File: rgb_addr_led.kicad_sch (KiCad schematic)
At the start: 64 parts

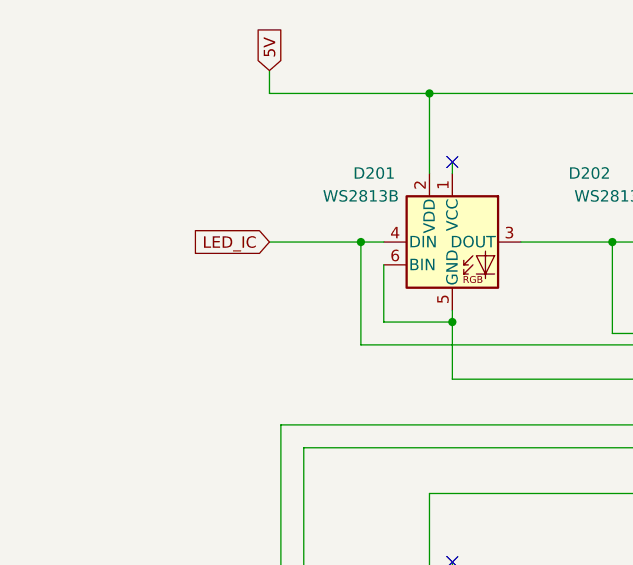
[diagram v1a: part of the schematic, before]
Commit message: add backup led data line with open solder bridge
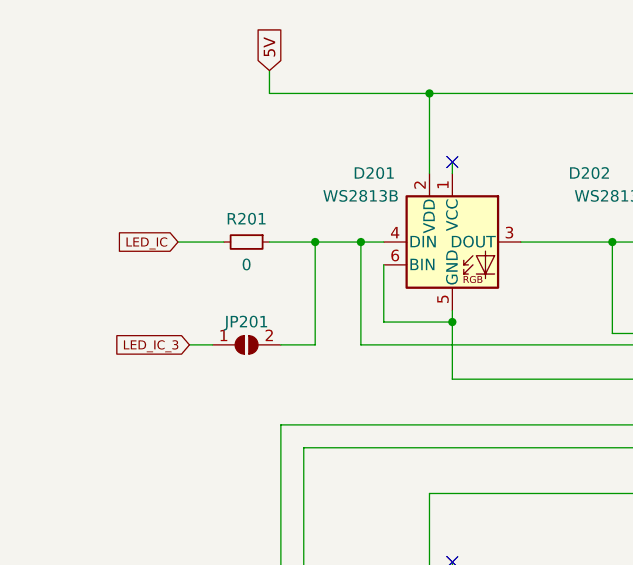
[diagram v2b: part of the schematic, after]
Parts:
- added JP201: SolderJumper_2_Open, Jumper:SolderJumper-2_P1.3mm_Open_TrianglePad1.0x1.5mm, symbol Jumper:SolderJumper_2_Open
- added R201: 0, Resistor_SMD:R_1206_3216Metric, symbol Device:R_Small
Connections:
- net LED_IC: now also R201.2; no longer D201.4 (DIN), D202.6 (BIN)
- new net: D201.4 (DIN), D202.6 (BIN), JP201.2 (B), R201.1
- new net LED_IC_3: JP201.1 (A)
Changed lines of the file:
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@@
   (junction (at 191.77 36.83) (diameter 0) (color 0 0 0 0)
   )
-  (junction (at 50.8 36.83) (diameter 0) (color 0 0 0 0)
-  )
   (junction (at 78.74 259.08) (diameter 0) (color 0 0 0 0)
   )
@@
   (junction (at 370.84 109.22) (diameter 0) (color 0 0 0 0)
   )
+  (junction (at 45.72 36.83) (diameter 0) (color 0 0 0 0)
+  )
   (junction (at 163.83 170.18) (diameter 0) (color 0 0 0 0)
   )
@@
   (junction (at 306.07 214.63) (diameter 0) (color 0 0 0 0)
   )
+  (junction (at 50.8 36.83) (diameter 0) (color 0 0 0 0)
+  )
   (junction (at 373.38 96.52) (diameter 0) (color 0 0 0 0)
   )
@@
     (stroke (width 0) (type default) (color 0 0 0 0))
   )
+  (wire (pts (xy 30.48 36.83) (xy 35.56 36.83))
+    (stroke (width 0) (type default) (color 0 0 0 0))
+  )
   (wire (pts (xy 78.74 214.63) (xy 78.74 224.79))
     (stroke (width 0) (type default) (color 0 0 0 0))
@@
     (stroke (width 0) (type default) (color 0 0 0 0))
   )
-  (wire (pts (xy 40.64 36.83) (xy 50.8 36.83))
-    (stroke (width 0) (type default) (color 0 0 0 0))
-  )
   (wire (pts (xy 344.17 27.94) (xy 344.17 29.21))
     (stroke (width 0) (type default) (color 0 0 0 0))
@@
     (stroke (width 0) (type default) (color 0 0 0 0))
   )
+  (wire (pts (xy 31.75 48.26) (xy 34.29 48.26))
+    (stroke (width 0) (type default) (color 0 0 0 0))
+  )
   (wire (pts (xy 308.61 48.26) (xy 278.13 48.26))
     (stroke (width 0) (type default) (color 0 0 0 0))
@@
     (stroke (width 0) (type default) (color 0 0 0 0))
   )
+  (wire (pts (xy 45.72 48.26) (xy 45.72 36.83))
+    (stroke (width 0) (type default) (color 0 0 0 0))
+  )
   (wire (pts (xy 41.91 81.28) (xy 49.53 81.28))
     (stroke (width 0) (type default) (color 0 0 0 0))
@@
     (stroke (width 0) (type default) (color 0 0 0 0))
   )
+  (wire (pts (xy 45.72 36.83) (xy 50.8 36.83))
+    (stroke (width 0) (type default) (color 0 0 0 0))
+  )
   (wire (pts (xy 116.84 250.19) (xy 116.84 251.46))
     (stroke (width 0) (type default) (color 0 0 0 0))
@@
     (stroke (width 0) (type default) (color 0 0 0 0))
   )
+  (wire (pts (xy 41.91 48.26) (xy 45.72 48.26))
+    (stroke (width 0) (type default) (color 0 0 0 0))
+  )
   (wire (pts (xy 256.54 153.67) (xy 256.54 162.56))
     (stroke (width 0) (type default) (color 0 0 0 0))
@@
     (stroke (width 0) (type default) (color 0 0 0 0))
   )
+  (wire (pts (xy 40.64 36.83) (xy 45.72 36.83))
+    (stroke (width 0) (type default) (color 0 0 0 0))
+  )
   (text "NOTE:" (at 13.97 77.47 0)
     (effects (font (size 1.27 1.27) (thickness 0.254) bold) (justify left bottom))
@@
     )
   )
-  (global_label "LED_IC" (shape input) (at 40.64 36.83 180) (fields_autoplaced)
-    (effects (font (size 1.27 1.27)) (justify right))
-    (property "Intersheet References" "${INTERSHEET_REFS}" (id 0) (at 31.9374 36.7506 0)
-      (effects (font (size 1.27 1.27)) (justify right) hide)
+  (global_label "LED_IC" (shape input) (at 30.48 36.83 180) (fields_autoplaced)
+    (effects (font (size 1 1)) (justify right))
+    (property "Intersheet References" "${INTERSHEET_REFS}" (id 0) (at 23.6276 36.7675 0)
+      (effects (font (size 1 1)) (justify right) hide)
+    )
+  )
+  (global_label "LED_IC_3" (shape input) (at 31.75 48.26 180) (fields_autoplaced)
+    (effects (font (size 1 1)) (justify right))
+    (property "Intersheet References" "${INTERSHEET_REFS}" (id 0) (at 23.1833 48.1975 0)
+      (effects (font (size 1 1)) (justify right) hide)
     )
   )
@@
     (pin "6")
   )
+  (symbol (lib_id "Device:R_Small") (at 38.1 36.83 270) (unit 1)
+    (in_bom yes) (on_board yes)
+    (property "Reference" "R201" (id 0) (at 38.1 34.29 90))
+    (property "Value" "0" (id 1) (at 38.1 39.37 90))
+    (property "Footprint" "Resistor_SMD:R_1206_3216Metric" (id 2) (at 38.1 36.83 0)
+      (effects (font (size 1.27 1.27)) hide)
+    )
+    (property "Datasheet" "~" (id 3) (at 38.1 36.83 0)
+      (effects (font (size 1.27 1.27)) hide)
+    )
+    (property "LCSC" "C17477" (id 4) (at 38.1 36.83 0)
+      (effects (font (size 1.27 1.27)) hide)
+    )
+    (pin "1")
+    (pin "2")
+  )
   (symbol (lib_id "LED:WS2813") (at 60.96 214.63 0) (unit 1)
     (in_bom yes) (on_board yes)
@@
     (pin "6")
   )
+  (symbol (lib_id "Jumper:SolderJumper_2_Open") (at 38.1 48.26 0) (unit 1)
+    (in_bom no) (on_board yes)
+    (property "Reference" "JP201" (id 0) (at 38.1 45.72 0))
+    (property "Value" "SolderJumper_2_Open" (id 1) (at 38.1 44.45 0)
+      (effects (font (size 1.27 1.27)) hide)
+    )
+    (property "Footprint" "Jumper:SolderJumper-2_P1.3mm_Open_TrianglePad1.0x1.5mm" (id 2) (at 38.1 48.26 0)
+      (effects (font (size 1.27 1.27)) hide)
+    )
+    (property "Datasheet" "~" (id 3) (at 38.1 48.26 0)
+      (effects (font (size 1.27 1.27)) hide)
+    )
+    (pin "1")
+    (pin "2")
+  )
   (symbol (lib_id "LED:WS2813") (at 116.84 259.08 0) (unit 1)

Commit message: update part number
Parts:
- R201: LCSC C17477 -> C17888
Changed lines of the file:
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@@
       (effects (font (size 1.27 1.27)) hide)
     )
-    (property "LCSC" "C17477" (id 4) (at 38.1 36.83 0)
+    (property "LCSC" "C17888" (id 4) (at 38.1 36.83 0)
       (effects (font (size 1.27 1.27)) hide)
     )

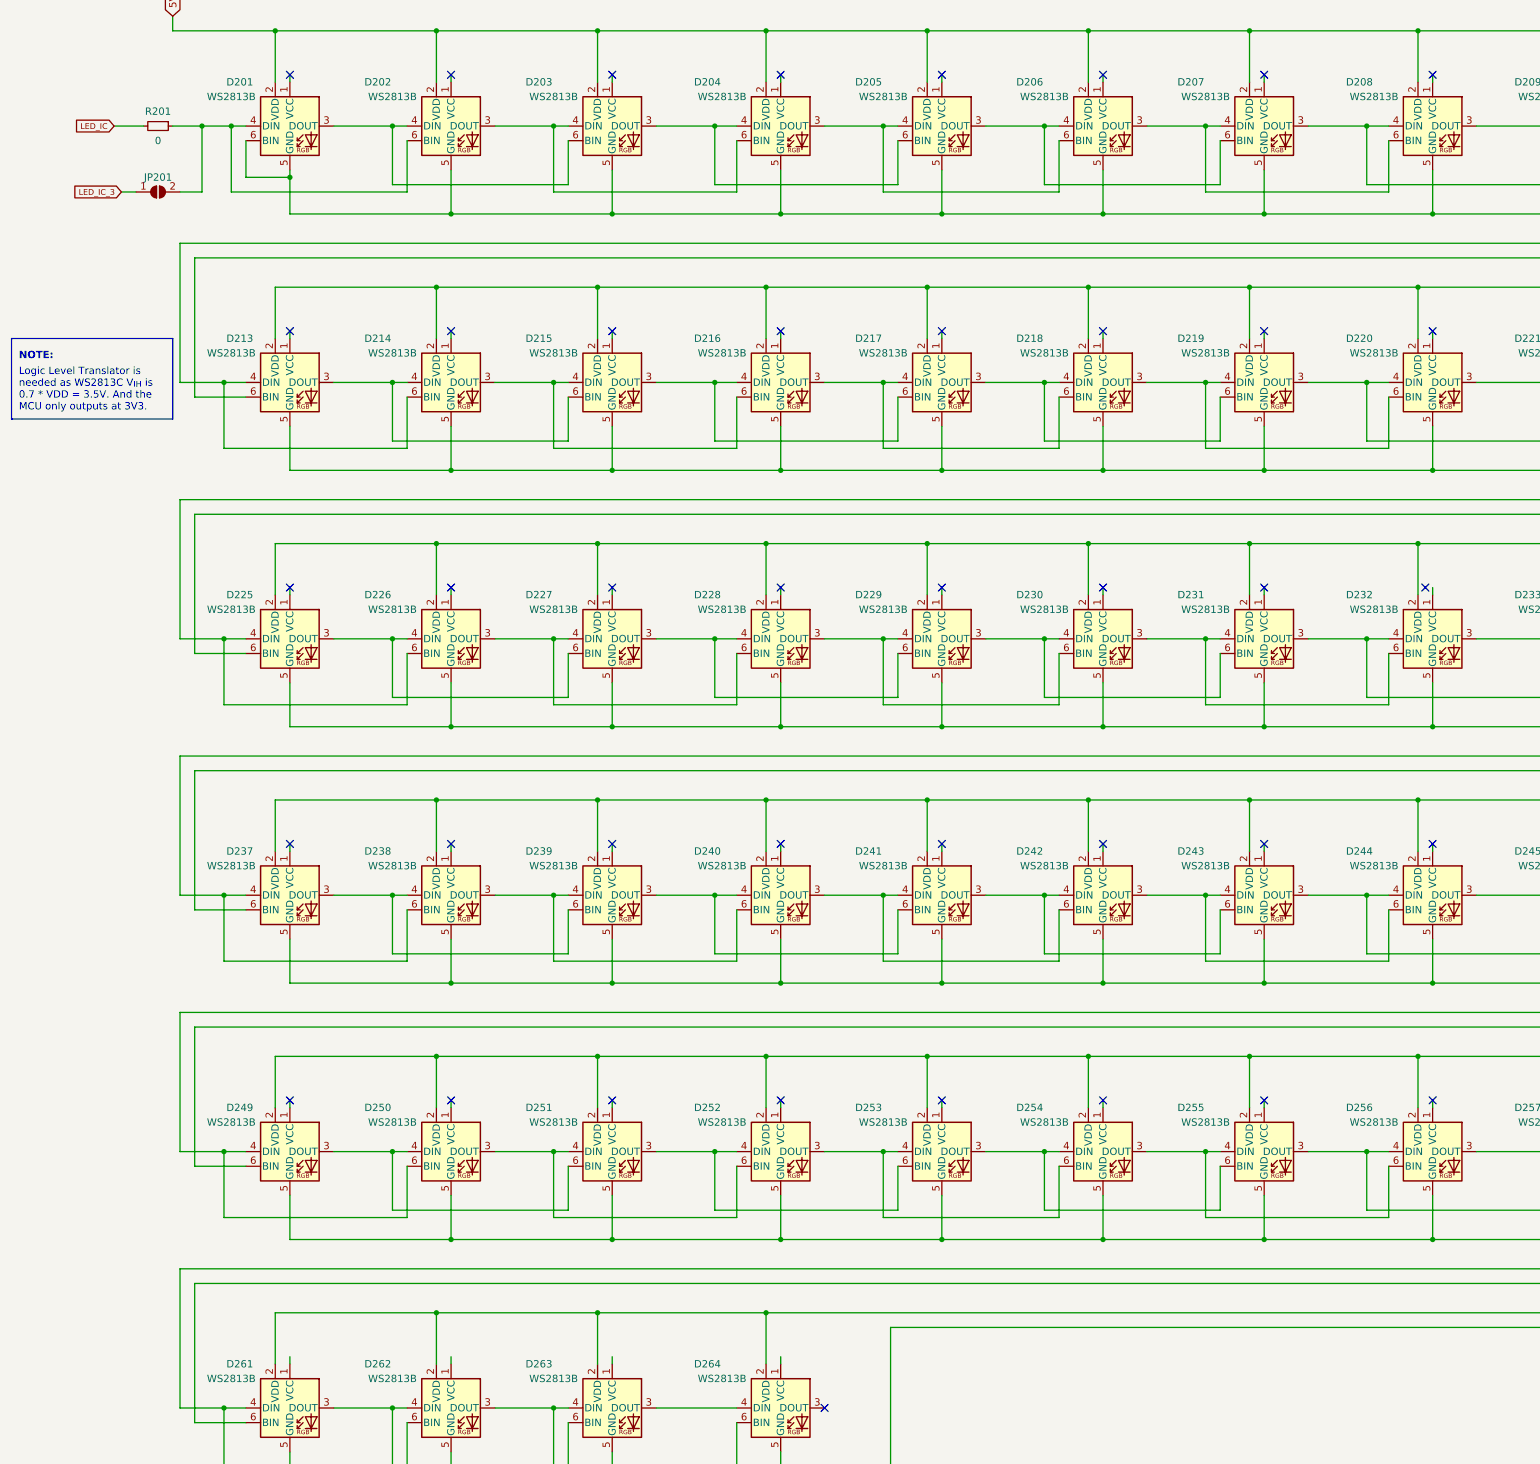
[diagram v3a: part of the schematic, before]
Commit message: fix issues in rev.b design
- fix connector design to fix potential crosstalk issues with LED data line causing unintentional LED light in the first LED in the array.
- combined all interrupts into single interrupt.
- add ground between each connector pin (to rid crosstalk).
- added in-line resistor to minimize crosstalk (33 ohms)
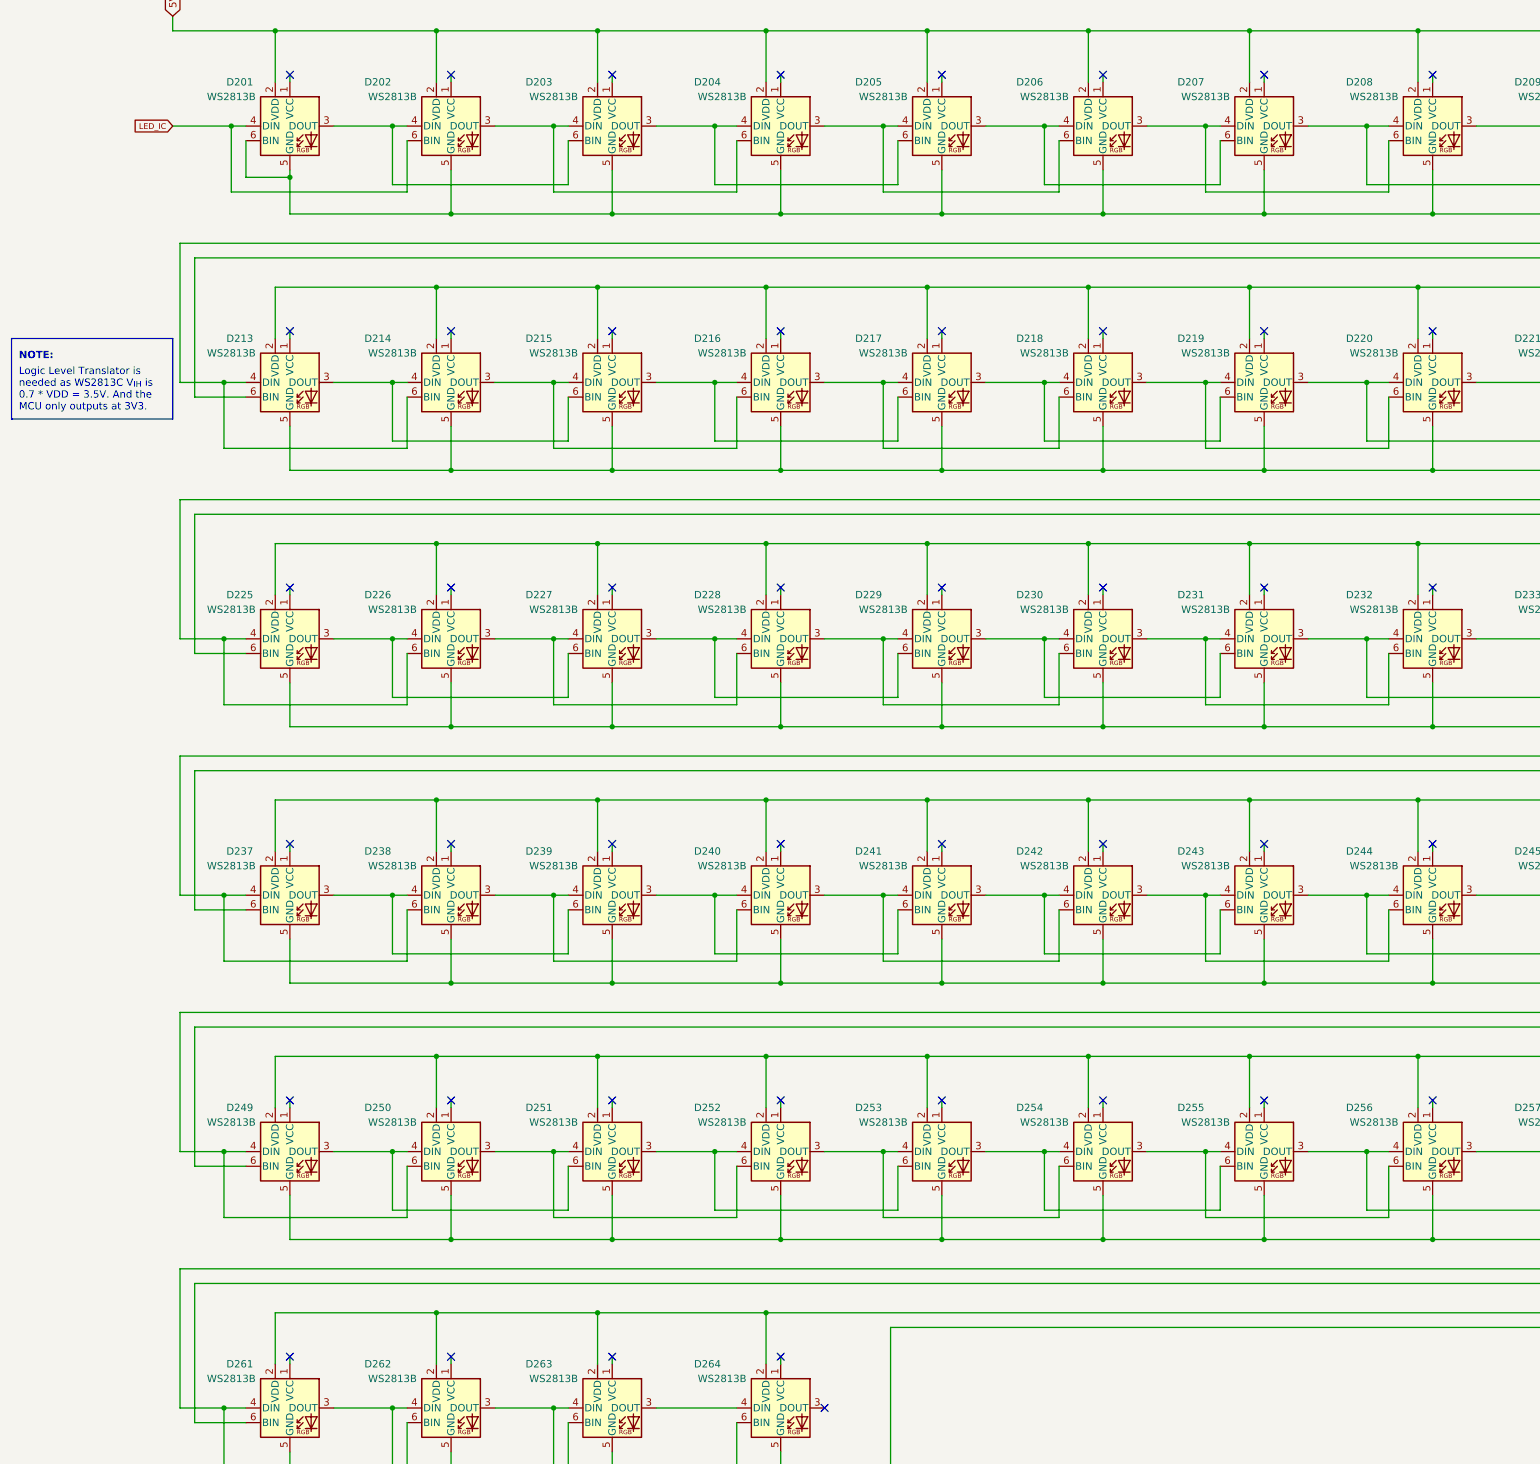
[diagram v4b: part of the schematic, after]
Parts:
- removed JP201: SolderJumper_2_Open, Jumper:SolderJumper-2_P1.3mm_Open_TrianglePad1.0x1.5mm, symbol Jumper:SolderJumper_2_Open
- removed R201: 0, Resistor_SMD:R_1206_3216Metric, symbol Device:R_Small
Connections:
- net LED_IC: now also D201.4 (DIN), D202.6 (BIN)
- no-connect marks 61 -> 65
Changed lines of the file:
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@@
   (junction (at 370.84 109.22) (diameter 0) (color 0 0 0 0)
   )
-  (junction (at 45.72 36.83) (diameter 0) (color 0 0 0 0)
-  )
   (junction (at 163.83 170.18) (diameter 0) (color 0 0 0 0)
   )
@@
   (junction (at 165.1 274.32) (diameter 0) (color 0 0 0 0)
   )
+  (no_connect (at 88.9 250.19))
+  (no_connect (at 60.96 250.19))
+  (no_connect (at 116.84 250.19))
+  (no_connect (at 146.05 250.19))
   (no_connect (at 88.9 27.94))
   (no_connect (at 116.84 27.94))
@@
   (no_connect (at 146.05 116.84))
   (no_connect (at 373.38 161.29))
-  (no_connect (at 257.81 116.84))
+  (no_connect (at 259.08 116.84))
   (no_connect (at 229.87 116.84))
   (no_connect (at 173.99 116.84))
@@
     (stroke (width 0) (type default) (color 0 0 0 0))
   )
+  (wire (pts (xy 40.64 20.32) (xy 58.42 20.32))
+    (stroke (width 0) (type default) (color 0 0 0 0))
+  )
   (wire (pts (xy 134.62 125.73) (xy 138.43 125.73))
     (stroke (width 0) (type default) (color 0 0 0 0))
@@
     (stroke (width 0) (type default) (color 0 0 0 0))
   )
-  (wire (pts (xy 40.64 20.32) (xy 58.42 20.32))
-    (stroke (width 0) (type default) (color 0 0 0 0))
-  )
   (wire (pts (xy 288.29 72.39) (xy 288.29 73.66))
     (stroke (width 0) (type default) (color 0 0 0 0))
@@
     (stroke (width 0) (type default) (color 0 0 0 0))
   )
-  (wire (pts (xy 30.48 36.83) (xy 35.56 36.83))
-    (stroke (width 0) (type default) (color 0 0 0 0))
-  )
   (wire (pts (xy 78.74 214.63) (xy 78.74 224.79))
     (stroke (width 0) (type default) (color 0 0 0 0))
@@
     (stroke (width 0) (type default) (color 0 0 0 0))
   )
-  (wire (pts (xy 31.75 48.26) (xy 34.29 48.26))
-    (stroke (width 0) (type default) (color 0 0 0 0))
-  )
   (wire (pts (xy 308.61 48.26) (xy 278.13 48.26))
     (stroke (width 0) (type default) (color 0 0 0 0))
@@
     (stroke (width 0) (type default) (color 0 0 0 0))
   )
-  (wire (pts (xy 45.72 48.26) (xy 45.72 36.83))
-    (stroke (width 0) (type default) (color 0 0 0 0))
-  )
   (wire (pts (xy 41.91 81.28) (xy 49.53 81.28))
     (stroke (width 0) (type default) (color 0 0 0 0))
@@
     (stroke (width 0) (type default) (color 0 0 0 0))
   )
-  (wire (pts (xy 45.72 36.83) (xy 50.8 36.83))
+  (wire (pts (xy 40.64 36.83) (xy 50.8 36.83))
     (stroke (width 0) (type default) (color 0 0 0 0))
   )
@@
     (stroke (width 0) (type default) (color 0 0 0 0))
   )
-  (wire (pts (xy 41.91 48.26) (xy 45.72 48.26))
-    (stroke (width 0) (type default) (color 0 0 0 0))
-  )
   (wire (pts (xy 256.54 153.67) (xy 256.54 162.56))
     (stroke (width 0) (type default) (color 0 0 0 0))
@@
     (stroke (width 0) (type default) (color 0 0 0 0))
   )
-  (wire (pts (xy 40.64 36.83) (xy 45.72 36.83))
-    (stroke (width 0) (type default) (color 0 0 0 0))
-  )
   (text "NOTE:" (at 13.97 77.47 0)
     (effects (font (size 1.27 1.27) (thickness 0.254) bold) (justify left bottom))
@@
     )
   )
-  (global_label "LED_IC" (shape input) (at 30.48 36.83 180) (fields_autoplaced)
-    (effects (font (size 1 1)) (justify right))
-    (property "Intersheet References" "${INTERSHEET_REFS}" (id 0) (at 23.6276 36.7675 0)
-      (effects (font (size 1 1)) (justify right) hide)
-    )
-  )
-  (global_label "LED_IC_3" (shape input) (at 31.75 48.26 180) (fields_autoplaced)
+  (global_label "LED_IC" (shape input) (at 40.64 36.83 180) (fields_autoplaced)
     (effects (font (size 1 1)) (justify right))
-    (property "Intersheet References" "${INTERSHEET_REFS}" (id 0) (at 23.1833 48.1975 0)
+    (property "Intersheet References" "${INTERSHEET_REFS}" (id 0) (at 33.7876 36.7675 0)
       (effects (font (size 1 1)) (justify right) hide)
     )
@@
     (pin "6")
   )
-  (symbol (lib_id "Device:R_Small") (at 38.1 36.83 270) (unit 1)
-    (in_bom yes) (on_board yes)
-    (property "Reference" "R201" (id 0) (at 38.1 34.29 90))
-    (property "Value" "0" (id 1) (at 38.1 39.37 90))
-    (property "Footprint" "Resistor_SMD:R_1206_3216Metric" (id 2) (at 38.1 36.83 0)
-      (effects (font (size 1.27 1.27)) hide)
-    )
-    (property "Datasheet" "~" (id 3) (at 38.1 36.83 0)
-      (effects (font (size 1.27 1.27)) hide)
-    )
-    (property "LCSC" "C17888" (id 4) (at 38.1 36.83 0)
-      (effects (font (size 1.27 1.27)) hide)
-    )
-    (pin "1")
-    (pin "2")
-  )
   (symbol (lib_id "LED:WS2813") (at 60.96 214.63 0) (unit 1)
     (in_bom yes) (on_board yes)
@@
     (pin "6")
   )
-  (symbol (lib_id "Jumper:SolderJumper_2_Open") (at 38.1 48.26 0) (unit 1)
-    (in_bom no) (on_board yes)
-    (property "Reference" "JP201" (id 0) (at 38.1 45.72 0))
-    (property "Value" "SolderJumper_2_Open" (id 1) (at 38.1 44.45 0)
-      (effects (font (size 1.27 1.27)) hide)
-    )
-    (property "Footprint" "Jumper:SolderJumper-2_P1.3mm_Open_TrianglePad1.0x1.5mm" (id 2) (at 38.1 48.26 0)
-      (effects (font (size 1.27 1.27)) hide)
-    )
-    (property "Datasheet" "~" (id 3) (at 38.1 48.26 0)
-      (effects (font (size 1.27 1.27)) hide)
-    )
-    (pin "1")
-    (pin "2")
-  )
   (symbol (lib_id "LED:WS2813") (at 116.84 259.08 0) (unit 1)
